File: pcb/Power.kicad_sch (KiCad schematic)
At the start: 96 parts, among them J4 Barrel_Jack, U1 LFE5U-85F-6BG381, U4 LTC4360-1, U5 SI1416EDH, U7 LTM8051

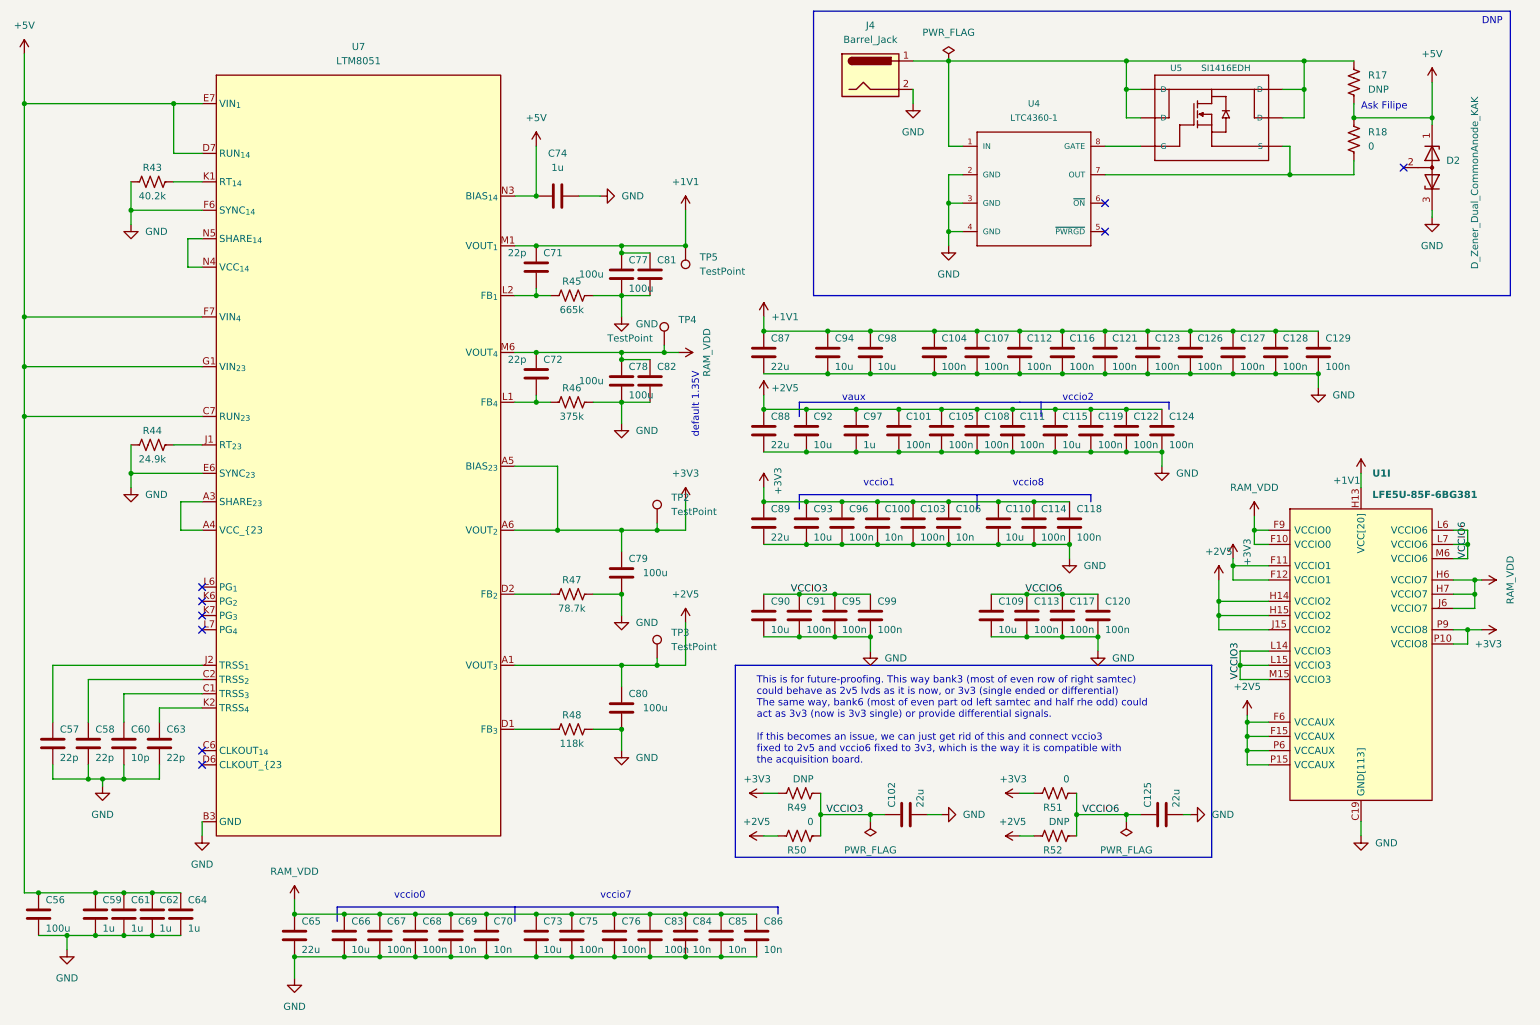
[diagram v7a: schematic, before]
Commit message: Initial footprint assignment
- Some edits to the schematic to improve readability
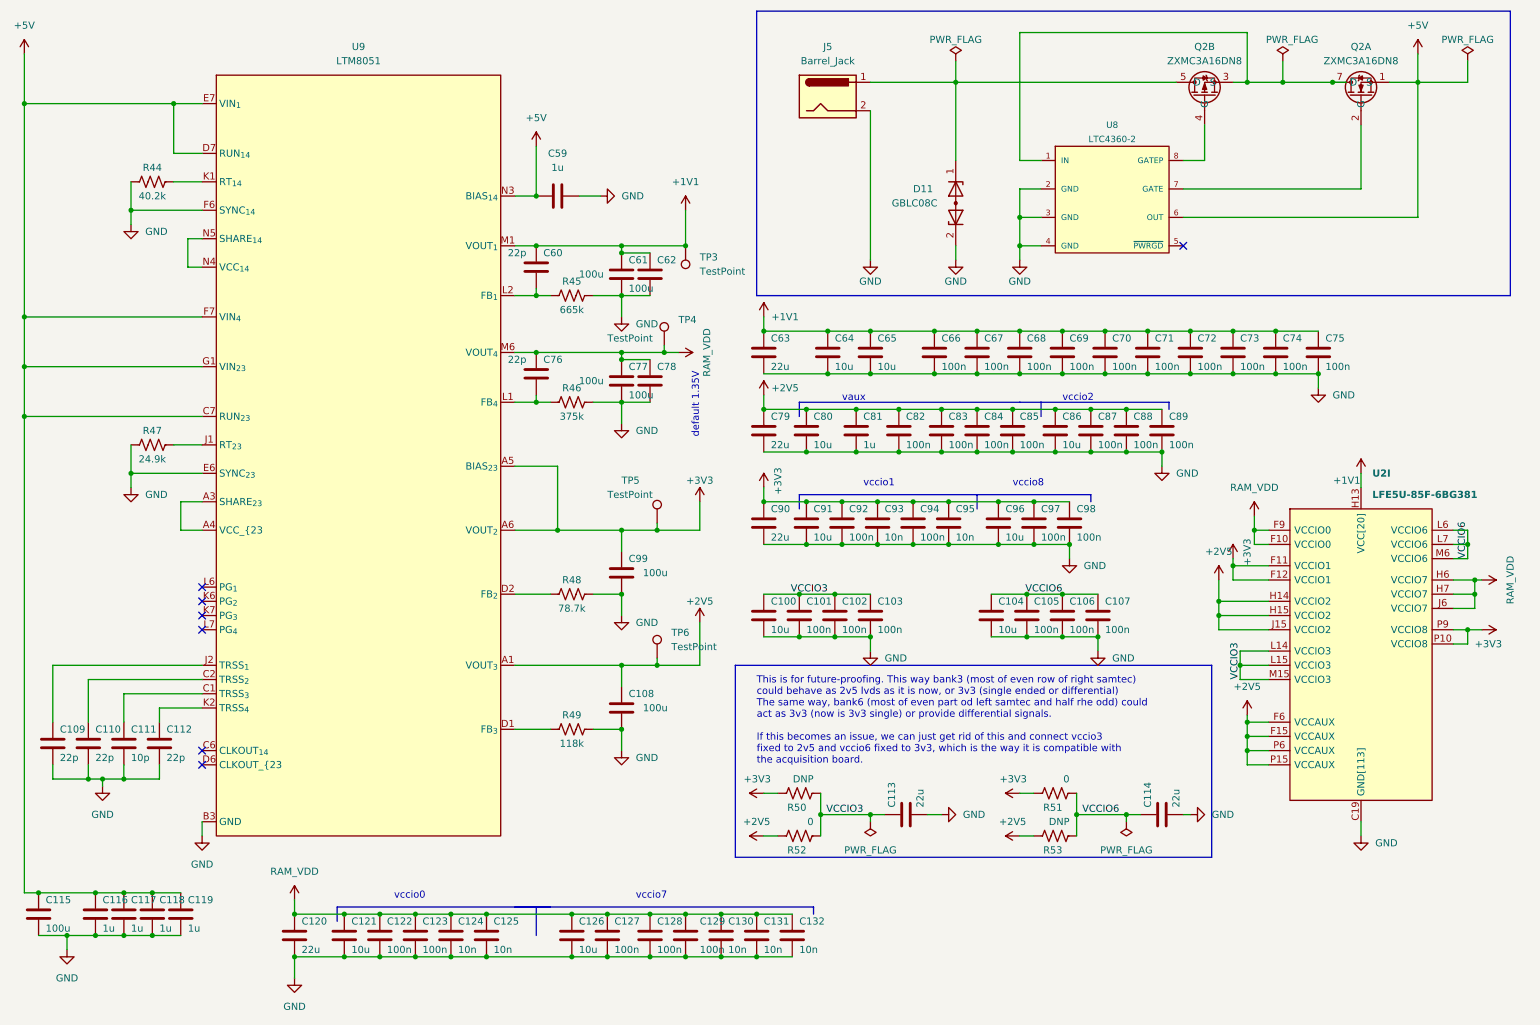
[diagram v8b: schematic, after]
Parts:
- removed D2: D_Zener_Dual_CommonAnode_KAK, symbol Device:D_Zener_Dual_CommonAnode_KAK
- removed R17: DNP, symbol Device:R_US
- removed R18: 0, symbol Device:R_US
- removed U4: LTC4360-1, LTC4360_SC70, symbol ecp5u85-bse-usb:LTC4360-1
- removed U5: SI1416EDH, SI1416EDH_SC-70-6L, symbol ecp5u85-bse-usb:SI1416EDH
- added D11: GBLC08C, Diode_SMD:D_SOD-323, symbol Device:D_Zener_Dual_CommonAnode_KAK
- added Q2: ZXMC3A16DN8, Package_SO:SO-8_3.9x4.9mm_P1.27mm, symbol ecp5u85-bse-usb:Dual_NMOS_PMOS
- added U8: LTC4360-2, Package_SO:SO-8_3.9x4.9mm_P1.27mm, symbol ecp5u85-bse-usb:LTC4360-2
- C100: renamed from C90; footprint (none) -> Capacitor_SMD:C_1210_3225Metric
- C101: renamed from C91; footprint (none) -> Capacitor_SMD:C_0402_1005Metric
- C102: renamed from C95; footprint (none) -> Capacitor_SMD:C_0402_1005Metric
- C103: renamed from C99; footprint (none) -> Capacitor_SMD:C_0402_1005Metric
- C104: renamed from C109; footprint (none) -> Capacitor_SMD:C_1210_3225Metric
- C105: renamed from C113; footprint (none) -> Capacitor_SMD:C_0402_1005Metric
- C106: renamed from C117; footprint (none) -> Capacitor_SMD:C_0402_1005Metric
- C107: renamed from C120; footprint (none) -> Capacitor_SMD:C_0402_1005Metric
- C108: renamed from C80; footprint (none) -> Capacitor_SMD:C_0402_1005Metric
- C109: renamed from C57; footprint (none) -> Capacitor_SMD:C_0402_1005Metric
- C110: renamed from C58; footprint (none) -> Capacitor_SMD:C_0402_1005Metric
- C111: renamed from C60; footprint (none) -> Capacitor_SMD:C_0402_1005Metric
- C112: renamed from C63; footprint (none) -> Capacitor_SMD:C_0402_1005Metric
- C113: renamed from C102; footprint (none) -> Capacitor_SMD:C_1210_3225Metric
- C114: renamed from C125; footprint (none) -> Capacitor_SMD:C_1210_3225Metric
- C115: renamed from C56; footprint (none) -> Capacitor_Tantalum_SMD:CP_EIA-3216-18_Kemet-A
- C116: renamed from C59; footprint (none) -> Capacitor_SMD:C_0805_2012Metric
- C117: renamed from C61; footprint (none) -> Capacitor_SMD:C_0805_2012Metric
- C118: renamed from C62; footprint (none) -> Capacitor_SMD:C_0805_2012Metric
- C119: renamed from C64; footprint (none) -> Capacitor_SMD:C_0805_2012Metric
- C120: renamed from C65; footprint (none) -> Capacitor_SMD:C_1210_3225Metric
- C121: renamed from C66; footprint (none) -> Capacitor_SMD:C_1210_3225Metric
- C122: renamed from C67; footprint (none) -> Capacitor_SMD:C_0402_1005Metric
- C123: renamed from C68; footprint (none) -> Capacitor_SMD:C_0402_1005Metric
- C124: renamed from C69; footprint (none) -> Capacitor_SMD:C_0402_1005Metric
- C125: renamed from C70; footprint (none) -> Capacitor_SMD:C_0402_1005Metric
- C126: renamed from C73; footprint (none) -> Capacitor_SMD:C_0402_1005Metric
- C127: renamed from C75; footprint (none) -> Capacitor_SMD:C_0402_1005Metric
- C128: renamed from C76; footprint (none) -> Capacitor_SMD:C_0402_1005Metric
- C129: renamed from C83; footprint (none) -> Capacitor_SMD:C_0402_1005Metric
- C130: renamed from C84; footprint (none) -> Capacitor_SMD:C_0402_1005Metric
- C131: renamed from C85; footprint (none) -> Capacitor_SMD:C_0402_1005Metric
- C132: renamed from C86; footprint (none) -> Capacitor_SMD:C_0402_1005Metric
- C59: renamed from C74; footprint (none) -> Capacitor_SMD:C_0805_2012Metric
- C60: renamed from C71; footprint (none) -> Capacitor_SMD:C_0402_1005Metric
- C61: renamed from C77; footprint (none) -> Capacitor_Tantalum_SMD:CP_EIA-3216-18_Kemet-A
- C62: renamed from C81; footprint (none) -> Capacitor_Tantalum_SMD:CP_EIA-3216-18_Kemet-A
- C63: renamed from C87; footprint (none) -> Capacitor_SMD:C_1210_3225Metric
- C64: renamed from C94; footprint (none) -> Capacitor_SMD:C_1210_3225Metric
- C65: renamed from C98; footprint (none) -> Capacitor_SMD:C_1210_3225Metric
- C66: renamed from C104; footprint (none) -> Capacitor_SMD:C_0402_1005Metric
- C67: renamed from C107; footprint (none) -> Capacitor_SMD:C_0402_1005Metric
- C68: renamed from C112; footprint (none) -> Capacitor_SMD:C_0402_1005Metric
- C69: renamed from C116; footprint (none) -> Capacitor_SMD:C_0402_1005Metric
- C70: renamed from C121; footprint (none) -> Capacitor_SMD:C_0402_1005Metric
- C71: renamed from C123; footprint (none) -> Capacitor_SMD:C_0402_1005Metric
- C72: renamed from C126; footprint (none) -> Capacitor_SMD:C_0402_1005Metric
- C73: renamed from C127; footprint (none) -> Capacitor_SMD:C_0402_1005Metric
- C74: renamed from C128; footprint (none) -> Capacitor_SMD:C_0402_1005Metric
- C75: renamed from C129; footprint (none) -> Capacitor_SMD:C_0402_1005Metric
- C76: renamed from C72; footprint (none) -> Capacitor_SMD:C_0402_1005Metric
- C77: renamed from C78; footprint (none) -> Capacitor_Tantalum_SMD:CP_EIA-3216-18_Kemet-A
- C78: renamed from C82; footprint (none) -> Capacitor_Tantalum_SMD:CP_EIA-3216-18_Kemet-A
- C79: renamed from C88; footprint (none) -> Capacitor_SMD:C_1210_3225Metric
- C80: renamed from C92; footprint (none) -> Capacitor_SMD:C_1210_3225Metric
- C81: renamed from C97; footprint (none) -> Capacitor_SMD:C_0805_2012Metric
- C82: renamed from C101; footprint (none) -> Capacitor_SMD:C_0402_1005Metric
- C83: renamed from C105; footprint (none) -> Capacitor_SMD:C_0402_1005Metric
- C84: renamed from C108; footprint (none) -> Capacitor_SMD:C_0402_1005Metric
- C85: renamed from C111; footprint (none) -> Capacitor_SMD:C_0402_1005Metric
- C86: renamed from C115; footprint (none) -> Capacitor_SMD:C_1210_3225Metric
- C87: renamed from C119; footprint (none) -> Capacitor_SMD:C_0402_1005Metric
- C88: renamed from C122; footprint (none) -> Capacitor_SMD:C_0402_1005Metric
- C89: renamed from C124; footprint (none) -> Capacitor_SMD:C_0402_1005Metric
- C90: renamed from C89; footprint (none) -> Capacitor_SMD:C_1210_3225Metric
- C91: renamed from C93; footprint (none) -> Capacitor_SMD:C_1210_3225Metric
- C92: renamed from C96; footprint (none) -> Capacitor_SMD:C_0402_1005Metric
- C93: renamed from C100; footprint (none) -> Capacitor_SMD:C_0402_1005Metric
- C94: renamed from C103; footprint (none) -> Capacitor_SMD:C_0402_1005Metric
- C95: renamed from C106; footprint (none) -> Capacitor_SMD:C_0402_1005Metric
- C96: renamed from C110; footprint (none) -> Capacitor_SMD:C_1210_3225Metric
- C97: renamed from C114; footprint (none) -> Capacitor_SMD:C_0402_1005Metric
- C98: renamed from C118; footprint (none) -> Capacitor_SMD:C_0402_1005Metric
- C99: renamed from C79; footprint (none) -> Capacitor_SMD:C_0402_1005Metric
- J5: renamed from J4; footprint (none) -> Connector_BarrelJack:BarrelJack_Horizontal
- R44: renamed from R43; footprint (none) -> Resistor_SMD:R_0402_1005Metric
- R45, R46, R51: footprint (none) -> Resistor_SMD:R_0402_1005Metric
- R47: renamed from R44; footprint (none) -> Resistor_SMD:R_0402_1005Metric
- R48: renamed from R47; footprint (none) -> Resistor_SMD:R_0402_1005Metric
- R49: renamed from R48; footprint (none) -> Resistor_SMD:R_0402_1005Metric
- R50: renamed from R49; footprint (none) -> Resistor_SMD:R_0402_1005Metric
- R52: renamed from R50; footprint (none) -> Resistor_SMD:R_0402_1005Metric
- R53: renamed from R52; footprint (none) -> Resistor_SMD:R_0402_1005Metric
- TP3: renamed from TP5; footprint (none) -> TestPoint:TestPoint_Pad_D1.0mm
- TP4: footprint (none) -> TestPoint:TestPoint_Pad_D1.0mm
- TP5: renamed from TP2; footprint (none) -> TestPoint:TestPoint_Pad_D1.0mm
- TP6: renamed from TP3; footprint (none) -> TestPoint:TestPoint_Pad_D1.0mm
- U2: renamed from U1; footprint Package_BGA:Lattice_caBGA-381_17.0x17.0mm_Layout20x20_P0.8mm_Ball0.4mm_Pad0.4mm_NSMD -> jonnew:LATTICE_caBGA-381_17.0x17.0mm
- U9: renamed from U7; footprint (none) -> jonnew:LINEAR_LTM8051
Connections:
- net +5V: now also Q2.1 (S), U8.6 (OUT)
- net GND: now also D11.2 (K), U8.2 (GND), U8.3 (GND), U8.4 (GND)
- net at J5.1: now also D11.1 (K), Q2.5 (D), Q2.6 (D)
- new net: Q2.2 (G), U8.7 (GATE)
- new net: Q2.3 (S), Q2.7 (D), Q2.8 (D), U8.1 (IN)
- new net: Q2.4 (G), U8.8 (GATEP)
- no-connect marks 9 -> 7
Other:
- note removed: "Ask Filipe"
- note removed: "DNP"
- company: OEPS -> OEPS & Open Ephys, Inc.
- title: ECP5U85-BSE-USB Breakout board -> ECP5U85-BSE-USB Breakout Board
- moved on the sheet: C126, C127, C128, C129, C130, C131, C132, J5
